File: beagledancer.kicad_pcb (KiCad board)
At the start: 2 copper layers, 32 x 23.1 mm, 12 parts, among them J1 USB-MICRO-B, P9 BeagleBone, U1 MAX3421, X1 XTAL4PIN

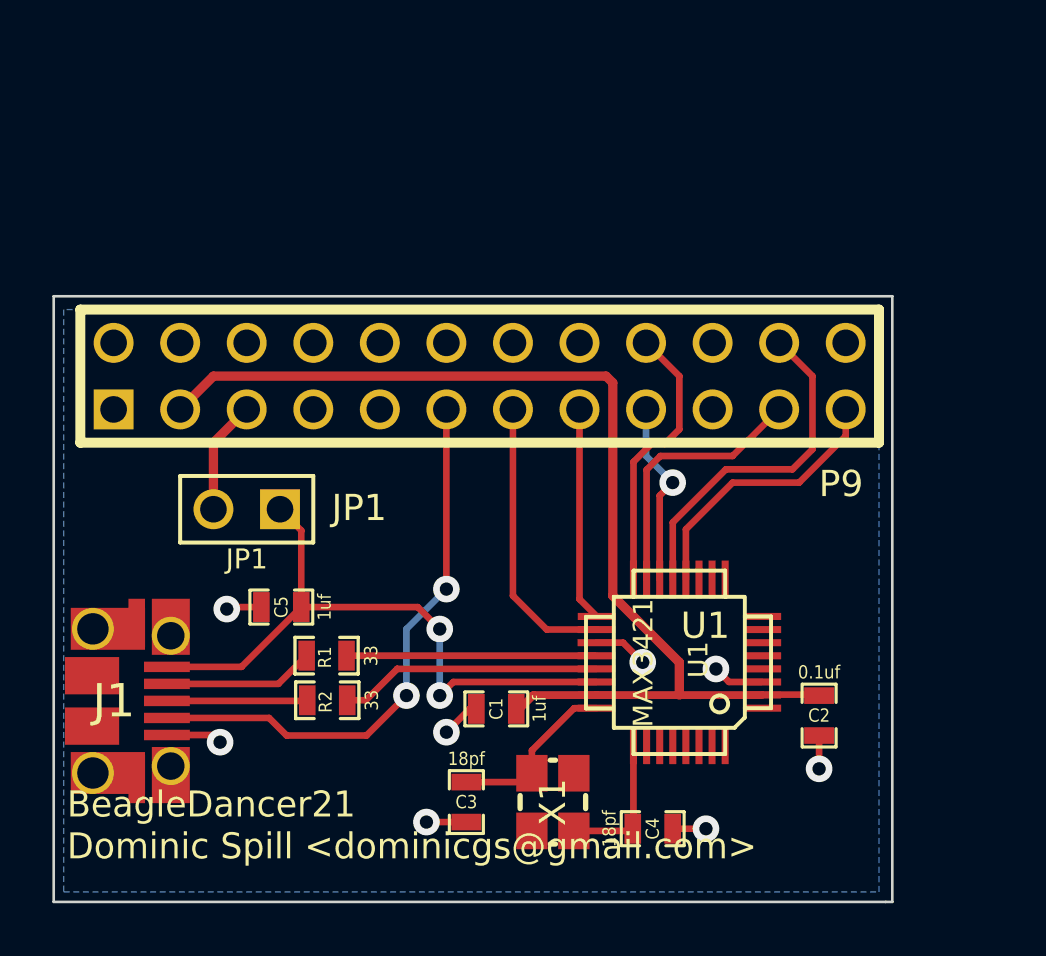
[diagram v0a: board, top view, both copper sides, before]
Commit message: Add a header for the RPi.
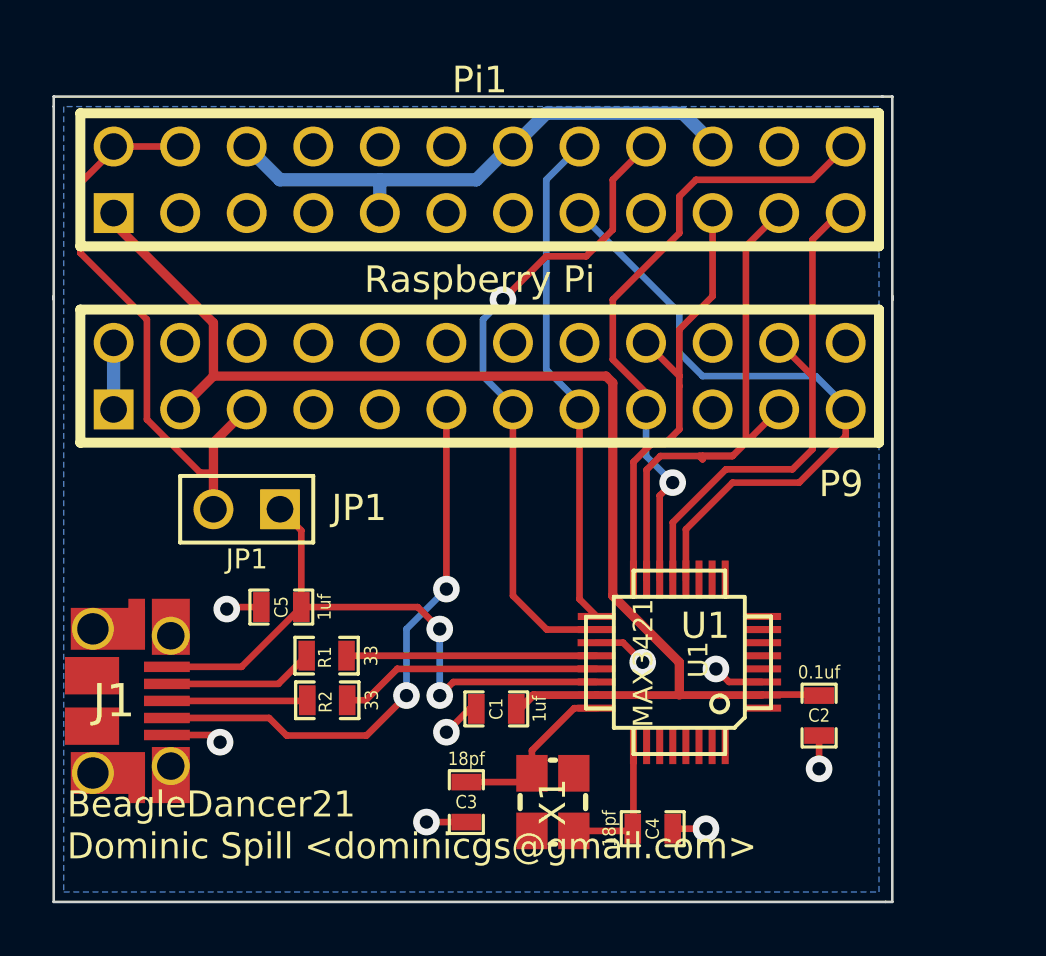
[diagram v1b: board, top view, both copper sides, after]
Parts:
- added Pi1: Raspberry Pi, pin_array_12x2, F.Cu at (214.6, 132.2)
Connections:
- net SPI0_CS0 renamed SPI_SS
- net SPI0_D0 renamed SPI_MISO
- net SPI0_D1 renamed SPI_MOSI
- net SPI0_SCLK renamed SPI_SCLK
- P9 pad 2: N-0000029 -> GND
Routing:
- net GND: track 13.2 -> 37.0 mm
- net +5V: track 4.34 -> 22.2 mm
- net SPI_SS: track 10.8 -> 27.7 mm
- net /RES: track 12.3 -> 26.5 mm
- net INT: track 11.2 -> 25.2 mm, vias 0 -> 1
- net GPX: track 8.18 -> 19.3 mm
- net SPI_MISO: track 14.2 -> 25.1 mm
- net +3.3V: track 41.8 -> 49.6 mm
- net SPI_MOSI: track 17.2 -> 23.9 mm
- net SPI_SCLK: track 15.3 -> 21.9 mm
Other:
- board size 32 x 23.1 mm -> 32 x 30.7 mm
- net class GND link added: clearance 0.2032, trace_width 0.508, via_dia 1.016, via_drill 0.508

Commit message: Update silkscreens and GND zone for RPi header.
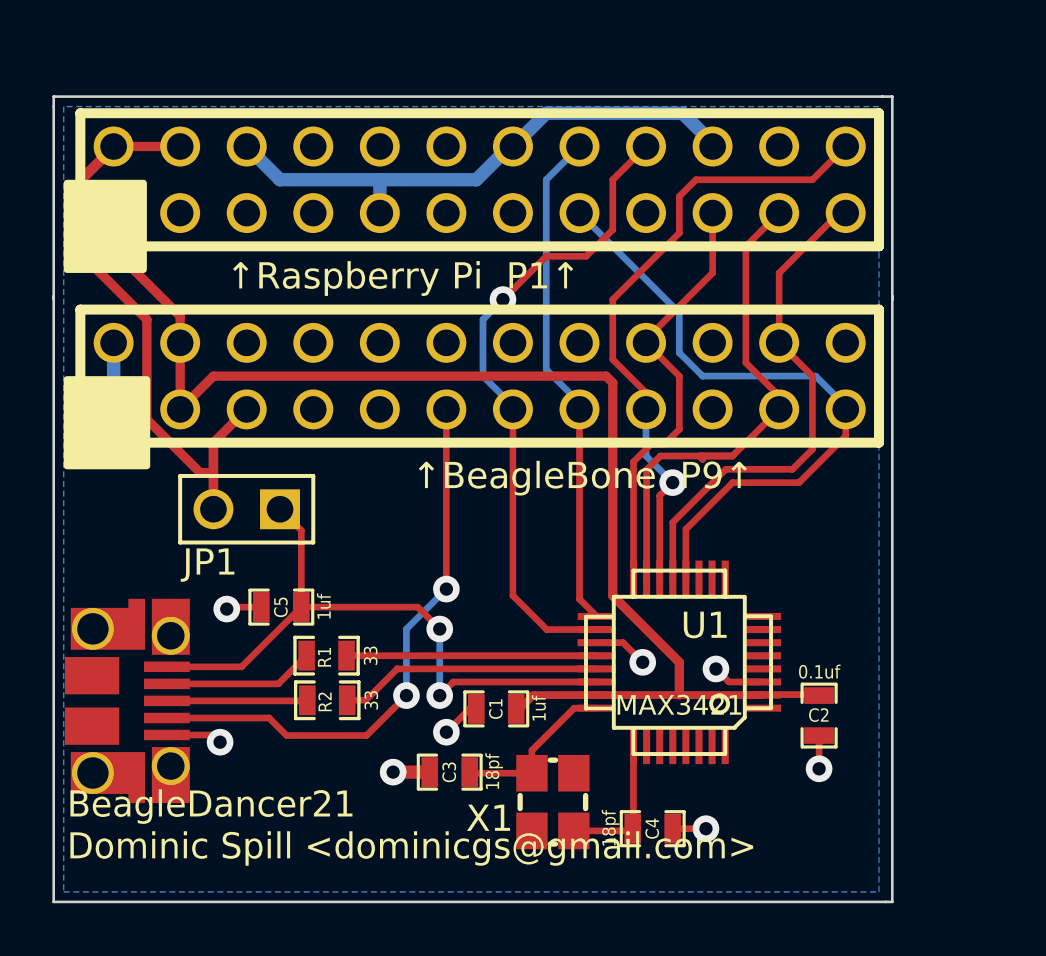
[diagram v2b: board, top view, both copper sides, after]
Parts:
- moved C3 1.31 mm to (213.5, 154.8), turned to 180 degrees
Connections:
- P9 pad 4: N-0000039 (its old number) -> +3.3V
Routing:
- net +5V: track 22.2 -> 29.4 mm
- net /XI: track 13.5 -> 10.9 mm
- net +3.3V: track 49.6 -> 50.7 mm
- net SPI_MISO: track 25.1 -> 24.4 mm
- net SPI_MOSI: track 23.9 -> 23.2 mm
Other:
- board text added: "X1"
- board text added: "↑BeagleBone P9↑"
- board text added: "↑Raspberry Pi P1↑"
- board text removed: "P9"
